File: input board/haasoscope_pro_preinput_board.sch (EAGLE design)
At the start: 43 parts, among them J2 8pin, J4 8pin, K1 AQY21SOP, K2 G6K-2F-RF-DC3, K3 G6K-2F-RF-DC3, K4 G6K-2F-RF-DC3, Q1 S8050, Q2 S8050, Q3 S8050

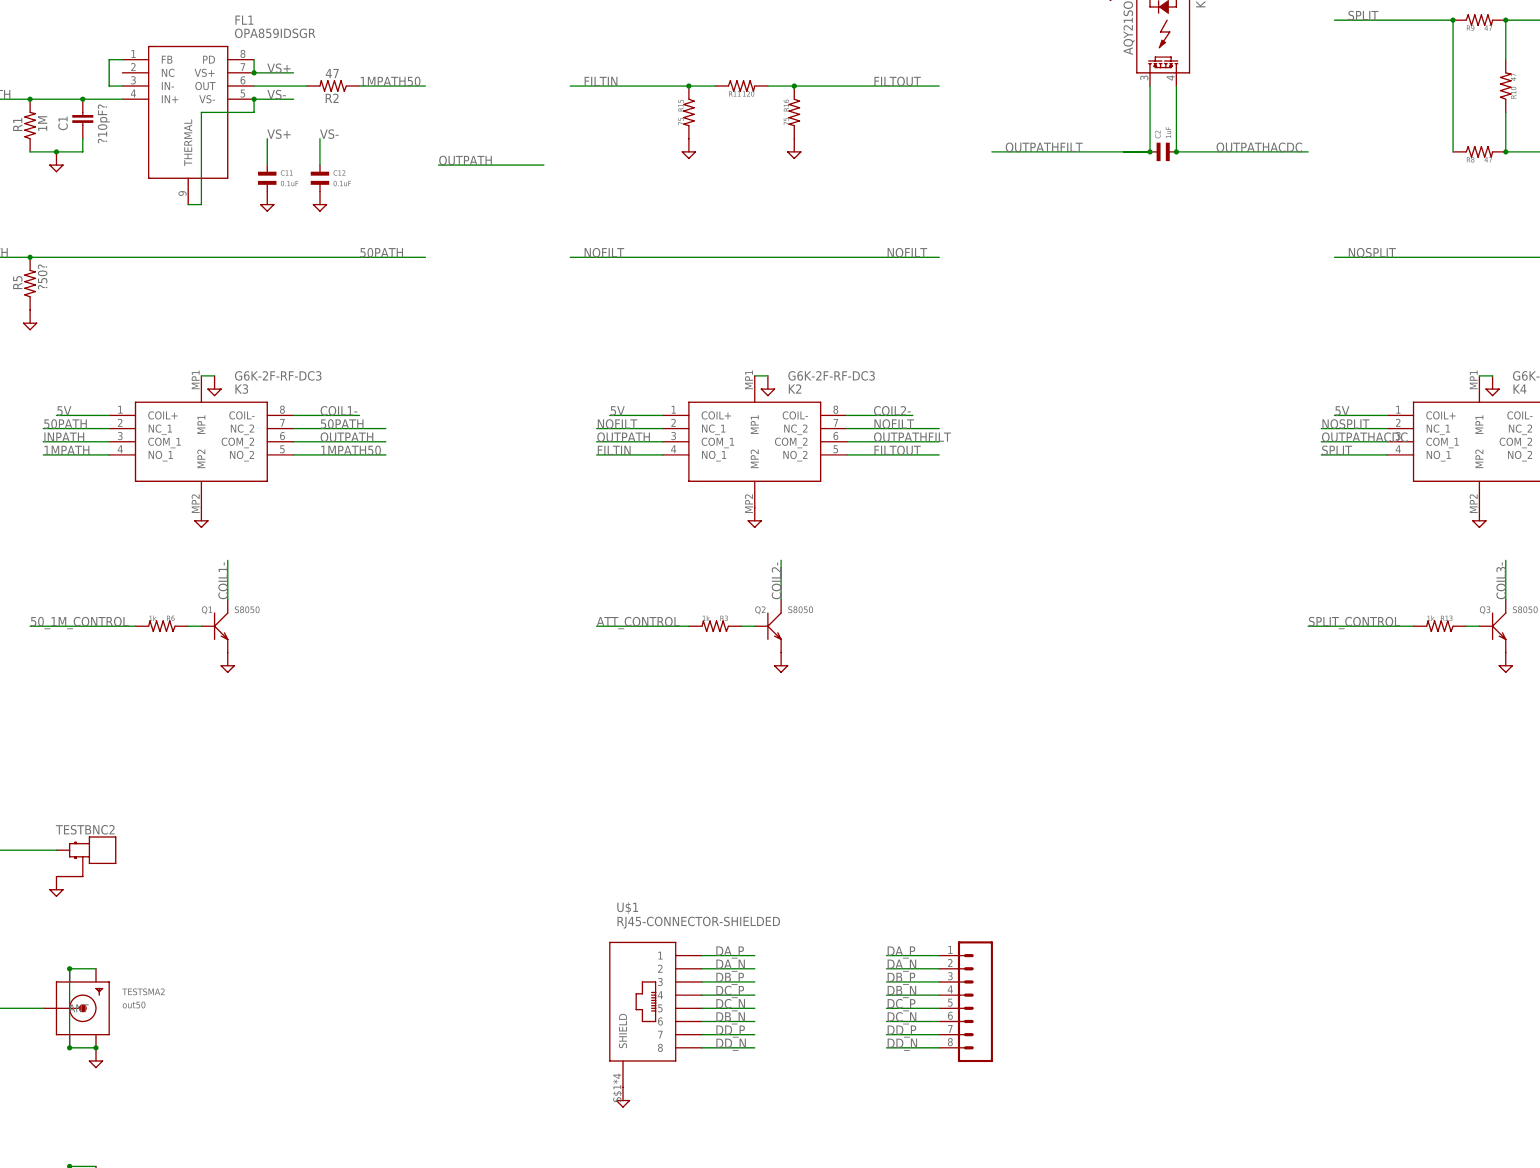
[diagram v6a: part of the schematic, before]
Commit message: add usb A port for powering probe
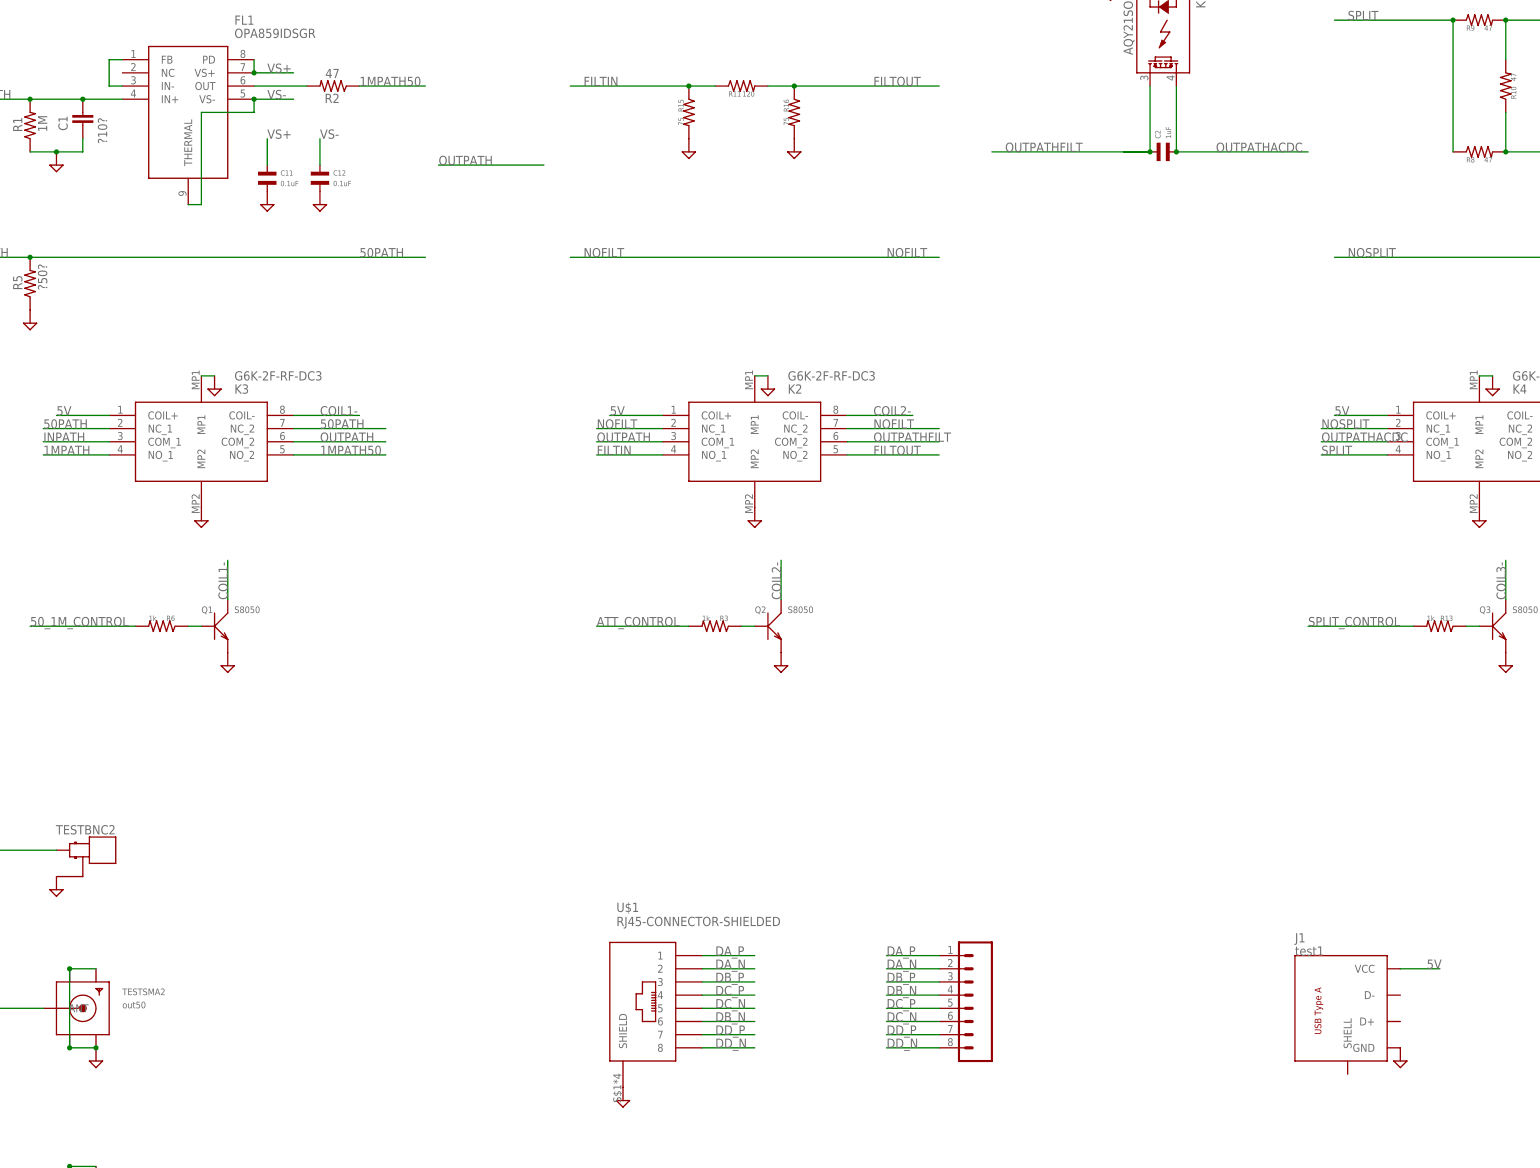
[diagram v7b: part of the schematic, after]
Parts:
- added J1: test1, FlashPCB_Connectors:USB-TYPE-ATHT-RA
- C1: value ?10pF? -> ?10?
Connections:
- net 5V: now also J1.VCC
- net GND: now also J1.GND
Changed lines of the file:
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@@
 <part name="FL1" library="OPA859IDSGR" deviceset="OPA859IDSGR" device=""/>
 <part name="R1" library="resistor" library_urn="urn:adsk.eagle:library:348" deviceset="R-US_" device="R0805" package3d_urn="urn:adsk.eagle:package:23553/2" value="1M"/>
-<part name="C1" library="resistor" library_urn="urn:adsk.eagle:library:348" deviceset="C-EU" device="C0805" package3d_urn="urn:adsk.eagle:package:23617/2" value="?10pF?"/>
+<part name="C1" library="resistor" library_urn="urn:adsk.eagle:library:348" deviceset="C-EU" device="C0805" package3d_urn="urn:adsk.eagle:package:23617/2" value="?10?"/>
 <part name="SUPPLY1" library="supply2" library_urn="urn:adsk.eagle:library:372" deviceset="GND" device=""/>
 <part name="R2" library="resistor" library_urn="urn:adsk.eagle:library:348" deviceset="R-US_" device="R0805" package3d_urn="urn:adsk.eagle:package:23553/2" value="47"/>
@@
 <part name="SUPPLY28" library="supply2" library_urn="urn:adsk.eagle:library:372" deviceset="GND" device=""/>
 <part name="J2" library="SparkFun-Connectors" library_urn="urn:adsk.eagle:library:513" deviceset="CONN_08" device="&quot;" package3d_urn="urn:adsk.eagle:package:38138/1" value="8pin"/>
+<part name="J1" library="FlashPCB_Connectors" deviceset="USB-TYPE-A" device="THT-RA" value="test1"/>
+<part name="SUPPLY30" library="supply2" library_urn="urn:adsk.eagle:library:372" deviceset="GND" device=""/>
 </parts>
 <sheets>
@@
 <instance part="SUPPLY28" gate="GND" x="363.22" y="-119.38" smashed="yes"/>
 <instance part="J2" gate="G$1" x="429.26" y="-99.06" smashed="yes" rot="R180"/>
+<instance part="J1" gate="G$1" x="505.46" y="-101.6" smashed="yes">
+<attribute name="NAME" x="492.76" y="-88.9" size="1.778" layer="95"/>
+<attribute name="VALUE" x="492.76" y="-91.44" size="1.778" layer="96"/>
+</instance>
+<instance part="SUPPLY30" gate="GND" x="513.08" y="-111.76" smashed="yes"/>
 </instances>
 <busses>
@@
 <pinref part="SUPPLY28" gate="GND" pin="GND"/>
 </segment>
+<segment>
+<pinref part="J1" gate="G$1" pin="GND"/>
+<pinref part="SUPPLY30" gate="GND" pin="GND"/>
+</segment>
 </net>
 <net name="VS+" class="0">
@@
 <pinref part="K4" gate="G$1" pin="COIL+"/>
 </segment>
-</net>
+<segment>
+<pinref part="J1" gate="G$1" pin="VCC"/>
+<wire x1="513.08" y1="-93.98" x2="520.7" y2="-93.98" width="0.1524" layer="91"/>
+<label x="518.16" y="-93.98" size="1.778" layer="95"/>
+</segment>
+</net>

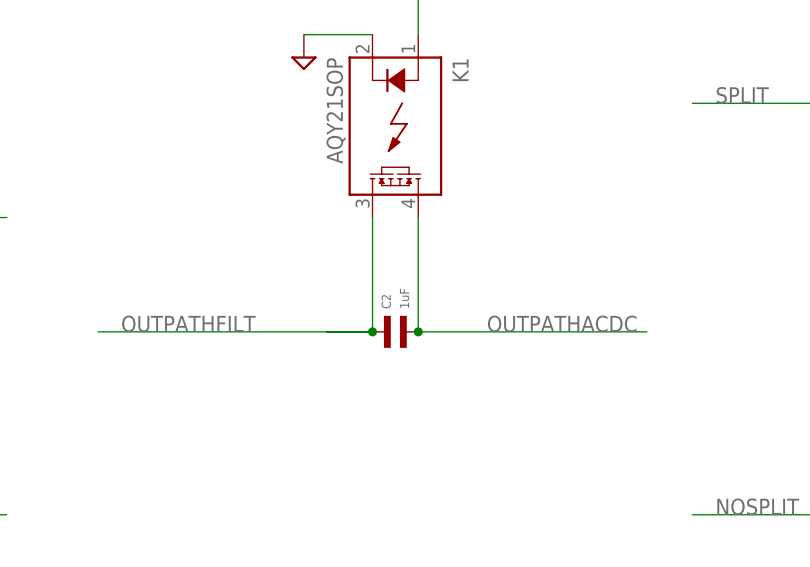
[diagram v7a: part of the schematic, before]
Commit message: specify rf dc blocking cap
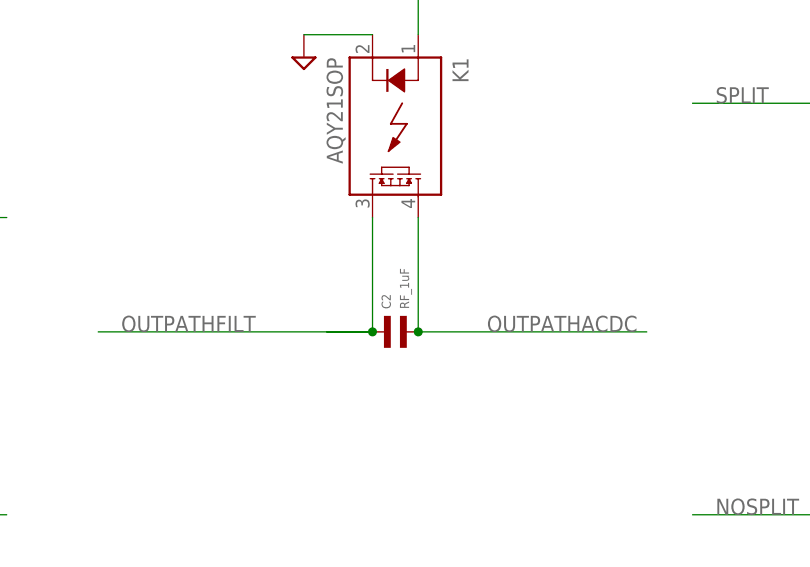
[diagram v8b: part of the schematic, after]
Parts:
- C2: value 1uF -> RF_1uF; LCSC (none) -> C52923
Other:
- note added: "Z~1.5 Ohm at 2 GHz for CL05A105KA5NQNC"
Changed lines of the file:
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@@
 <part name="R9" library="MF_Passives" deviceset="RESISTOR" device="_0402" value="47"/>
 <part name="R10" library="MF_Passives" deviceset="RESISTOR" device="_0402" value="47"/>
-<part name="C2" library="MF_Passives" deviceset="CAPACITOR_NP" device="_0402" value="1uF"/>
+<part name="C2" library="MF_Passives" deviceset="CAPACITOR_NP" device="_0402" value="RF_1uF">
+<attribute name="LCSC" value="C52923"/>
+</part>
 <part name="SUPPLY7" library="supply2" library_urn="urn:adsk.eagle:library:372" deviceset="GND" device=""/>
 <part name="Q3" library="Seeed-Transistor" library_urn="urn:adsk.eagle:library:477" deviceset="SMD-TRANSISTORS-NPN-25V-500MW-S8050(SOT-23)" device="" package3d_urn="urn:adsk.eagle:package:33015/1" value="S8050">
@@
 <text x="510.54" y="-17.78" size="1.778" layer="90">RF relay driver
 for splitting</text>
+<text x="454.66" y="55.88" size="1.778" layer="90">Z~1.5 Ohm at 2 GHz
+for CL05A105KA5NQNC</text>
 </plain>
 <instances>
@@
 <attribute name="NAME" x="465.836" y="66.04" size="1.016" layer="95" font="vector" rot="R90" align="top-left"/>
 <attribute name="VALUE" x="468.884" y="66.04" size="1.016" layer="96" font="vector" rot="R90"/>
+<attribute name="LCSC" x="467.36" y="63.5" size="1.778" layer="96" rot="R90" display="off"/>
 </instance>
 <instance part="SUPPLY7" gate="GND" x="528.32" y="-7.62" smashed="yes"/>
